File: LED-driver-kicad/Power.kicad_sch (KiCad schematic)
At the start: 32 parts, among them J1 Barrel_Jack, Q2 Q_NMOS_DGS, U1 PD70210A

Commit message: update Power schematic
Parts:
- added C10, C14: 10u, symbol Device:C_Small
- added C11, C15: 100n, symbol Device:C_Small
- added C12: 7u5, symbol Device:C_Small
- added C16: 1u8, symbol Device:C_Small
- added D6 (x2): D_Schottky, symbol Device:D_Schottky_Small_Filled
- added L2: 36u, symbol Device:L_Small
- added L3: 78u, symbol Device:L_Small
- added R24, R27: 100k, symbol Device:R_Small
- added R25: 33k, symbol Device:R_Small
- added R26, R29: 10k, symbol Device:R_Small
- added R28: 360k, symbol Device:R_Small
- added U1, U3: LV2862XLVDDCR, Package_SOT_SMD:SOT-23-Thin-6_DDC0006A-MFG_Regulator_Voltage_TI_LV2862XLVDDCR, symbol Regulator_Voltage_TI_LV2862XLVDDCR:LV2862XLVDDCR
- C5: value C_Small -> 4u7
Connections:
- net +3.3V: now also C12.1, L2.2, R25.1
- net GND: now also C10.2, C12.2, C14.2, C16.2, D6.2 (A), D6.2 (A), R26.2, R29.2, U1.2 (GND), U3.2 (GND); no longer C4.2, C6.2, D2.3 (-), D7.3 (-), JP1.2 (B), R17.2, R18.2, R21.2, U1.15 (WA_EN), U1.17 (ePAD), U1.7 (VPN_IN), U1.8 (VPN_IN)
- net OUTP+: now also C10.1, C14.1, R24.1, R27.1, U1.5 (VIN), U3.5 (VIN)
- net RJ45_VC1+: now also C2.1, D2.4, D9.2 (A), RV1.1; no longer C2.2, D2.2, D8.2 (A), RV2.2
- net RJ45_VC1-: now also C2.2, D2.2, D8.2 (A), RV2.2; no longer C2.1, D2.4, D9.2 (A), RV1.1
- net RJ45_VC2+: now also C3.1, D10.2 (A), D7.4, RV3.1; no longer C3.2, D11.2 (A), D7.2, RV4.2
- net RJ45_VC2-: now also C3.2, D11.2 (A), D7.2, RV4.2; no longer C3.1, D10.2 (A), D7.4, RV3.1
- new net: R28.2, R29.1, U3.3 (FB)
- new net: R25.2, R26.1, U1.3 (FB)
- new net: C15.2, D6.1 (K), L3.1, U3.6 (SW)
- new net: R24.2, U1.4 (~{SHDN})
- new net: R27.2, U3.4 (~{SHDN})
- new net: C11.1, U1.1 (CB)
- new net: C11.2, D6.1 (K), L2.1, U1.6 (SW)
- new net: C15.1, U3.1 (CB)
- new net +12V: C16.1, L3.2, R28.1
- new net OUTN-: C4.2, C6.2, D2.3 (-), D7.3 (-), JP1.2 (B), R17.2, R18.2, R21.2, U1.15 (WA_EN), U1.17 (ePAD), U1.7 (VPN_IN), U1.8 (VPN_IN)
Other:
- note added: "(WA_EN is not used)"
- note added: "12V Power"
- note added: "25AA02E64 - EEPROM w/ MAC address Supply Voltage (V_{CC}): 1.8V <= V_{CC} <= 5.5V Operating current (I_{CCREAD}): (V_{CC}=2.5V, F_{CLK}=5.0MHZ) -> (V_{CC}=5.5V, F_{CLK}=10.0MHZ) 2.5mA <= I_{CCREAD} <= 5mA Operating current (I_{CCWRITE}): 3mA <= I_{CCWRITE} <= 5mA"
- note added: "3V3 Power"
- note added: "AN3468 - Designing a PoE PD using PD702x0 and PD701x0 - See pg 20 for details on PCB layout. IEEE 802.3at Type 2 Guaranteed pwer at PD input: 25.50W PD input voltage: 42.5V to 57V Max DC current at PD input: 600mA max Supported physical layer classification class: Class 4 mandatory RCLS resistor (R17: ${767cd28d-739f-4f67-9bf1-3f1f92823cb1:VALUE}) values: 133 Ω, 69.8 Ω, 45.3 Ω, and 30.9 Ω for Cla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"
- note added: "ENC28J60 - Ethernet PHY Supply voltage (V_{DD}): 3.1V <= V_{DD} <= 3.6V 3.3V typical Operating current (I_{DD}): 180mA max 160mA typical"
- note added: "If 4-pair flags are used"
- note added: "MIC3205 - LED Driver Supply voltage (V_{IN}): 4.5V <= V_{IN} <= 40V (operating) -0.32V <= V_{IN} to PGND <= 42V (MAX) Supply current (I_{S}): 1.3mA typical 3mA (MAX)"
- note added: "PD70210A - PoE Controller Supply voltage (V_{PP}): 0V <= V_{PP} <= 57V (operating) -0.3V <= V_{PP} <=74V (MAX) Input current (I_{IN}): (@V_{PP}=55V) 1mA <= I_{IN} <= 3mA"
- note added: "PIC16F18026 - MCU 1.8V <= V_{DD} <= 5.5V -0.3V <= V_{DD} <= 6.5V (MAX) 3.3V typical Max current: 120mA <= I_{SS} <= 300mA 85mA <= I_{DD} <= 250mA"
- note added: "VAUX"
- note added: "VPP"
- note added: "VPP RTN"
- note added: "VPP: 42.5V to 57V (48V typical)"
- note removed: "(WA_EN not used)"
- note removed: "RCLS resistor (R17: ${767cd28d-739f-4f67-9bf1-3f1f92823cb1:VALUE}) values: 133 Ω, 69.8 Ω, 45.3 Ω, and 30.9 Ω for Class 1, 2, 3, and 4, respectively"
- note removed: "This may have to be a different ground. Analog ground? See datasheet."
- moved on the sheet: C10, C2, C3, C4, C5, C6, C9, D10, D11, D12, D2, D7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

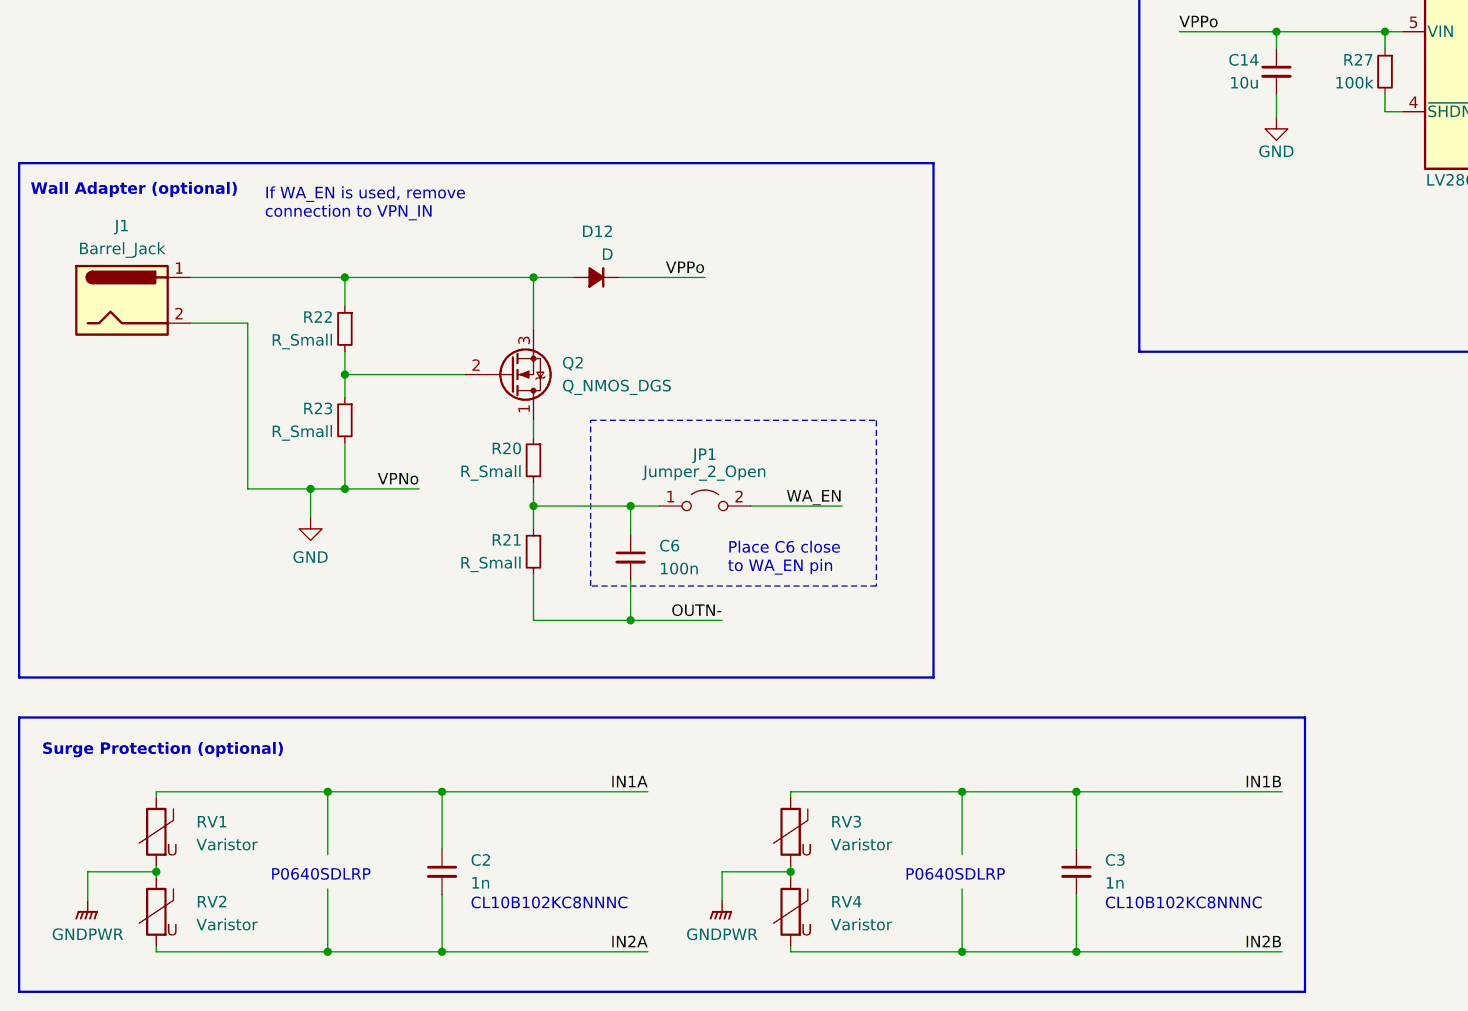
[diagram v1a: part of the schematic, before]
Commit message: remove surge protection and wall adapter circuit
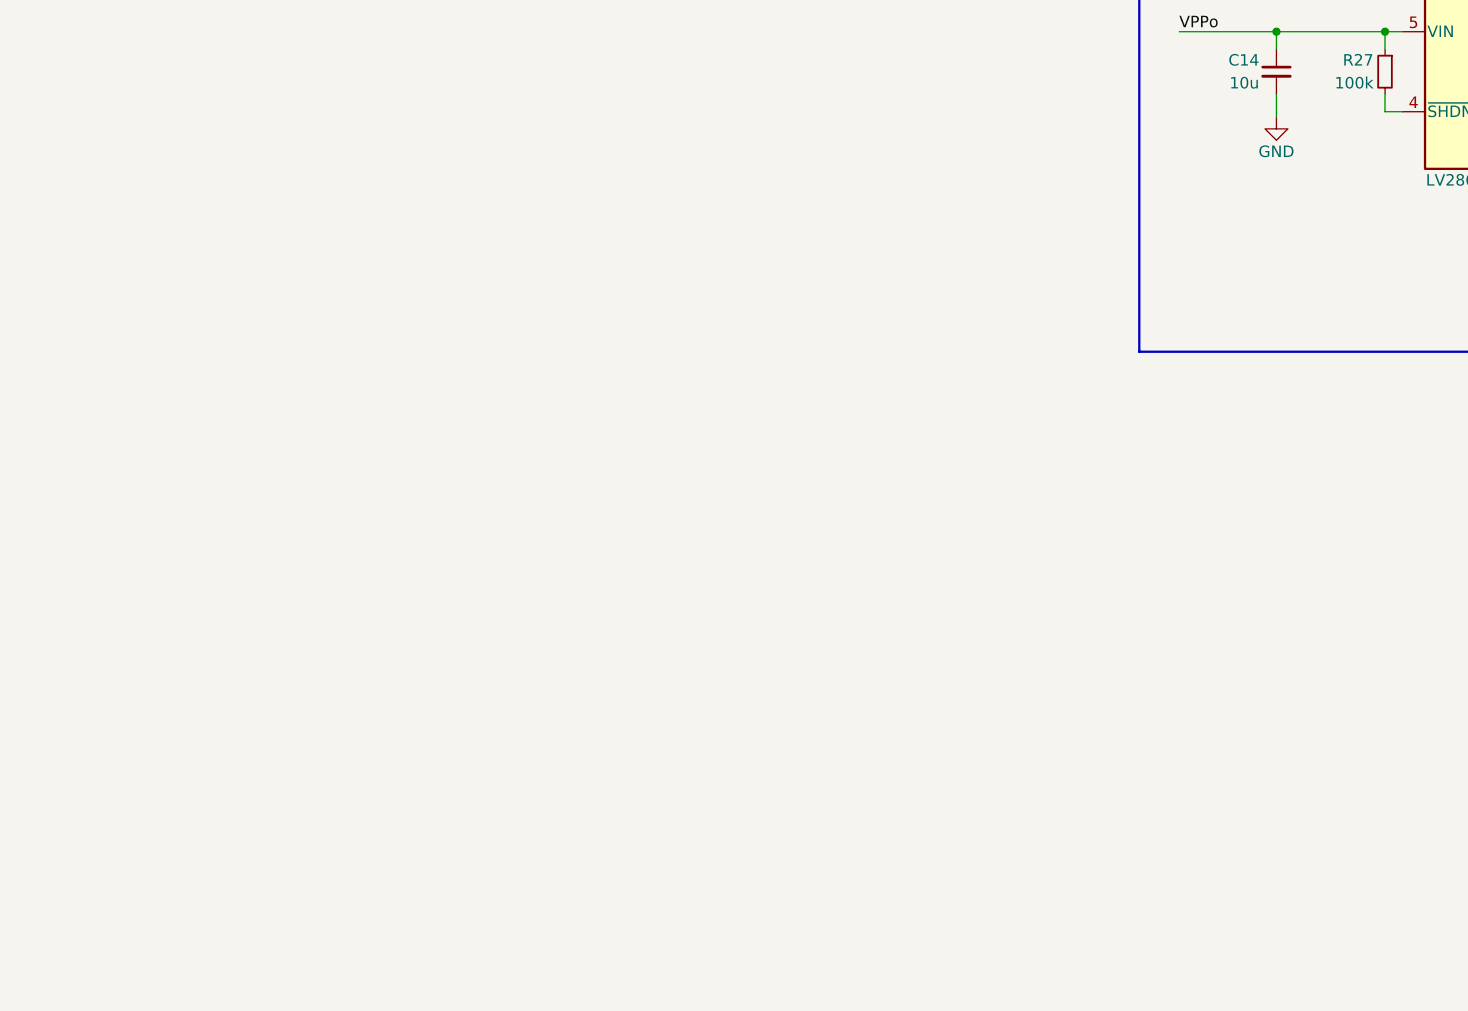
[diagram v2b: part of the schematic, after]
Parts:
- removed C2, C3: 1n, symbol Device:C_Small
- removed C6: 100n, symbol Device:C_Small
- removed D12: D, symbol Device:D_Small_Filled
- removed J1: Barrel_Jack, symbol Connector:Barrel_Jack
- removed JP1: Jumper_2_Open, symbol Jumper:Jumper_2_Open
- removed Q2: Q_NMOS_DGS, symbol Device:Q_NMOS_DGS
- removed R20, R21, R22, R23: R_Small, symbol Device:R_Small
- removed RV1, RV2, RV3, RV4: Varistor, symbol Device:Varistor
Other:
- note removed: "CL10B102KC8NNNC"
- note removed: "If WA_EN is used, remove connection to VPN_IN"
- note removed: "P0640SDLRP"
- note removed: "Place C6 close to WA_EN pin"
- note removed: "Surge Protection (optional)"
- note removed: "Wall Adapter (optional)"

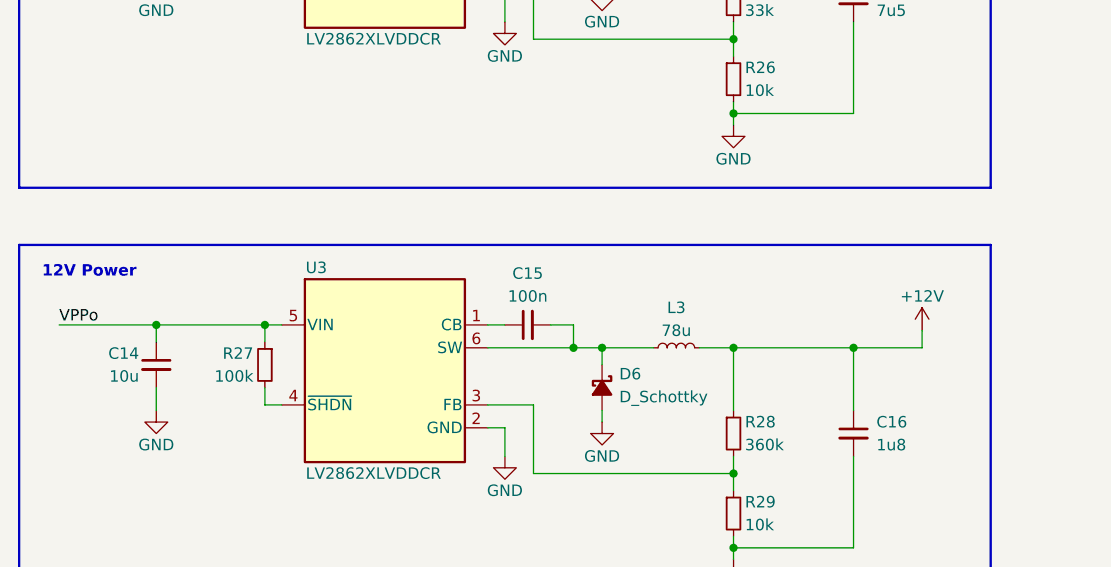
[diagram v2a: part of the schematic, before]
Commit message: update RGB LED driver circuits
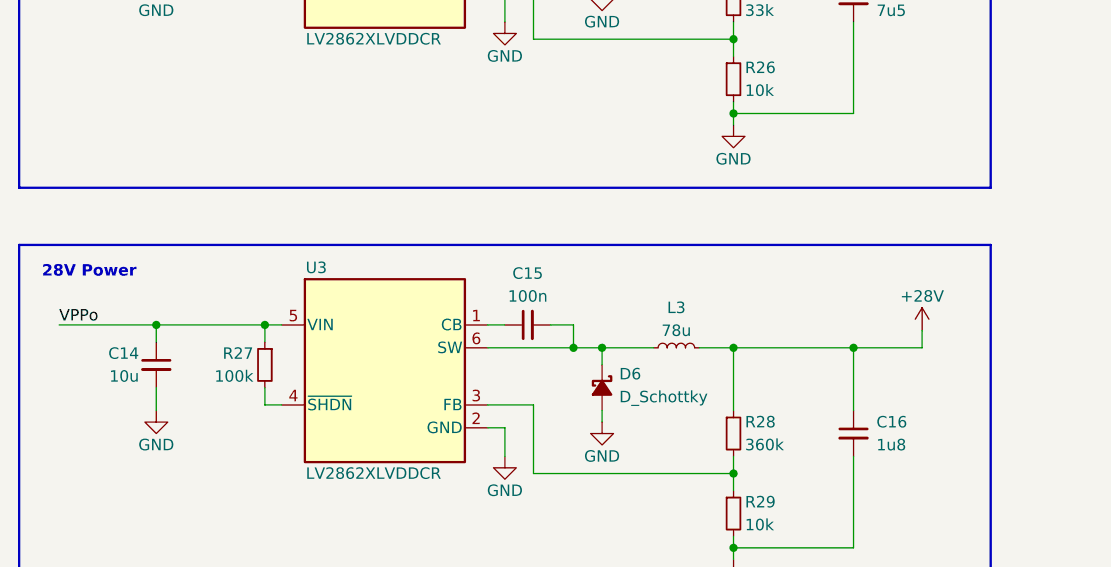
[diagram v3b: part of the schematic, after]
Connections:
- net +12V renamed +28V
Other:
- note added: "28V Power"
- note removed: "12V Power"
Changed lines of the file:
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@@
     (effects (font (size 1.27 1.27)) (justify left bottom))
   )
-  (text "12V Power" (at 21.59 137.16 0)
+  (text "28V Power" (at 21.59 137.16 0)
     (effects (font (size 1.27 1.27) (thickness 0.254) bold) (justify left bottom))
   )
@@
     )
   )
-  (symbol (lib_id "power:+12V") (at 119.38 142.875 0) (unit 1)
-    (in_bom yes) (on_board yes) (dnp no)
-    (property "Reference" "#PWR050" (at 119.38 146.685 0)
-      (effects (font (size 1.27 1.27)) hide)
-    )
-    (property "Value" "+12V" (at 119.38 139.065 0)
-      (effects (font (size 1.27 1.27)))
-    )
-    (property "Footprint" "" (at 119.38 142.875 0)
-      (effects (font (size 1.27 1.27)) hide)
-    )
-    (property "Datasheet" "" (at 119.38 142.875 0)
-      (effects (font (size 1.27 1.27)) hide)
-    )
-    (pin "1")
-    (instances
-      (project "LED-driver-kicad"
-        (path "/2b071084-2ab6-4896-84cc-45b211479417/21b4adef-5629-4a8b-8f2a-398551c789e3"
-          (reference "#PWR050") (unit 1)
-        )
-      )
-    )
-  )
   (symbol (lib_id "Device:C_Small") (at 234.95 35.56 0) (unit 1)
     (in_bom yes) (on_board yes) (dnp no) (fields_autoplaced)
@@
         )
       )
+    )
+  )
+  (symbol (lib_id "power:+28V") (at 119.38 142.875 0) (unit 1)
+    (in_bom yes) (on_board yes) (dnp no)
+    (property "Reference" "#PWR03" (at 119.38 146.685 0)
+      (effects (font (size 1.27 1.27)) hide)
+    )
+    (property "Value" "+28V" (at 119.38 139.065 0)
+      (effects (font (size 1.27 1.27)))
+    )
+    (property "Footprint" "" (at 125.73 141.605 0)
+      (effects (font (size 1.27 1.27)) hide)
+    )
+    (property "Datasheet" "" (at 125.73 141.605 0)
+      (effects (font (size 1.27 1.27)) hide)
+    )
+    (pin "1")
+    (instances
+      (project "LED-driver-kicad"
+        (path "/2b071084-2ab6-4896-84cc-45b211479417/250319e1-deb8-4d57-8ee9-fb5c0c792a75"
+          (reference "#PWR03") (unit 1)
+        )
+        (path "/2b071084-2ab6-4896-84cc-45b211479417/21b4adef-5629-4a8b-8f2a-398551c789e3"
+          (reference "#PWR011") (unit 1)
+        )
+      )

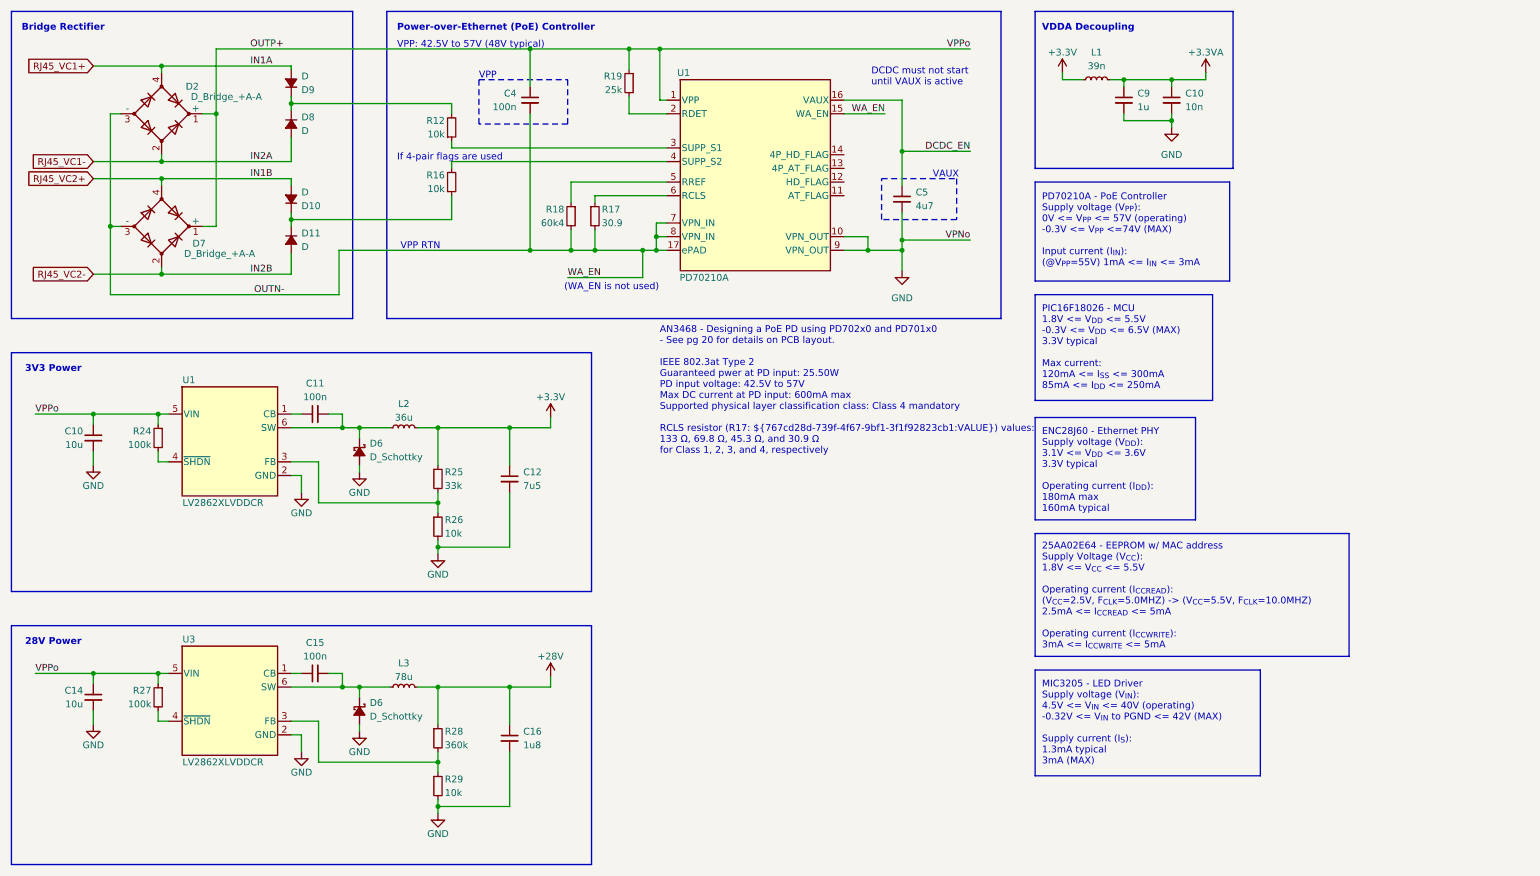
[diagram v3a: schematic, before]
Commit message: remove VDDA decoupling
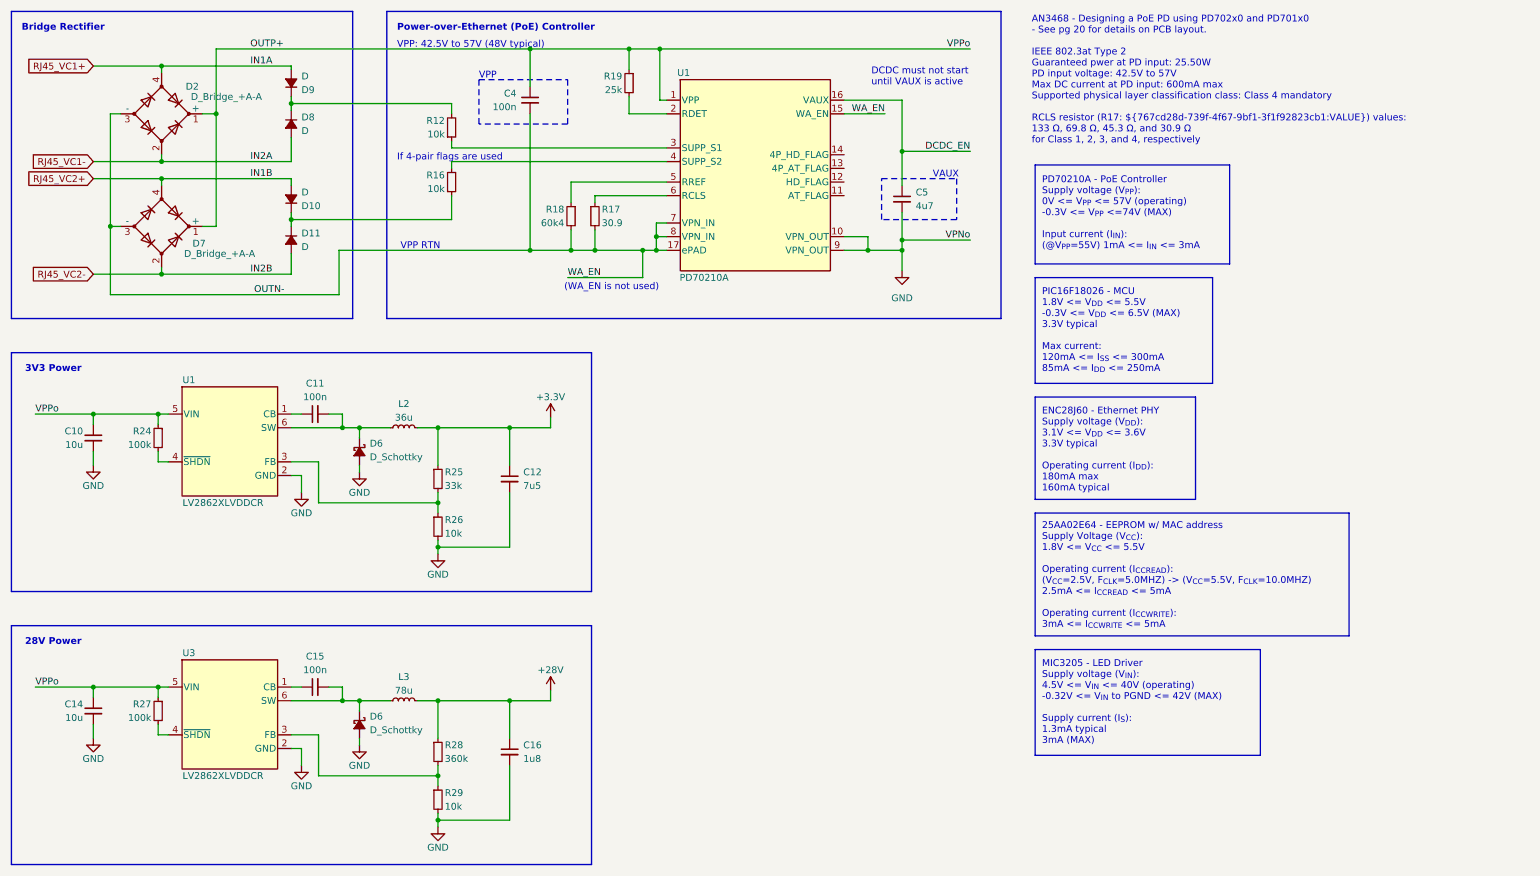
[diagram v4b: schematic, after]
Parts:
- removed C10: 10n, symbol Device:C_Small
- removed C9: 1u, symbol Device:C_Small
- removed L1: 39n, symbol Device:L_Small
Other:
- note removed: "VDDA Decoupling"
- moved on the sheet: C14, C15, C16, D6, L3, R27, R28, R29, U3

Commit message: update comments and title blocks
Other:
- title: (none) -> Photogrammetry Rig - LED Driver
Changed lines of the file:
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@@
 (kicad_sch (version 20230121) (generator eeschema)
   (paper "A4")
+  (title_block
+    (title "Photogrammetry Rig - LED Driver")
+    (date "2023-08-02")
+    (rev "0.1.0")
+  )
   (junction (at 98.425 147.32) (diameter 0) (color 0 0 0 0)
   )
